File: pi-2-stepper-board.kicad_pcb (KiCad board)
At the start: 2 copper layers, 65 x 56 mm, 18 parts, among them CON1 DC12v, P1 Servo (A0), P2 Endstop1 (A1), P3 Endstop2 (A2), P4 Stepper1, P5 Stepper2, P6 COM, P7 Aux (D10 - 13), SW1 GPIO21, SW2 ON - OFF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

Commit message: Added I2C updated text
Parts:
- added REF**: Symbol_OSHW-Logo_SilkScreen, Symbols:Symbol_OSHW-Logo_SilkScreen, B.Cu at (86.0, 61.8)
- SW1: value GPIO21 -> SW_PUSH
- SW2: value ON - OFF -> SPDT
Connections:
- U1 pad 3: Net-(U1-Pad3) -> /SDA
- U1 pad 5: Net-(U1-Pad5) -> /SCL
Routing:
- net /SDA: track 0.00 -> 49.5 mm, vias 0 -> 1
- net /SCL: track 0.00 -> 33.0 mm, vias 0 -> 1
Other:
- board text added: "Copyright Mark Benson 2016 License: CC-BY-NC"
- board text added: "Designed for use with Pycupi: https://github.com/brianinnes/pycupi"
- board text added: "Rapsberry Pi 2/3 Arduino Pro Mini (3.3v @ 8MHz) Dual Stepper control brd."
- board text added: "https://github.com/MarkJB/pi-2-stepper-board"

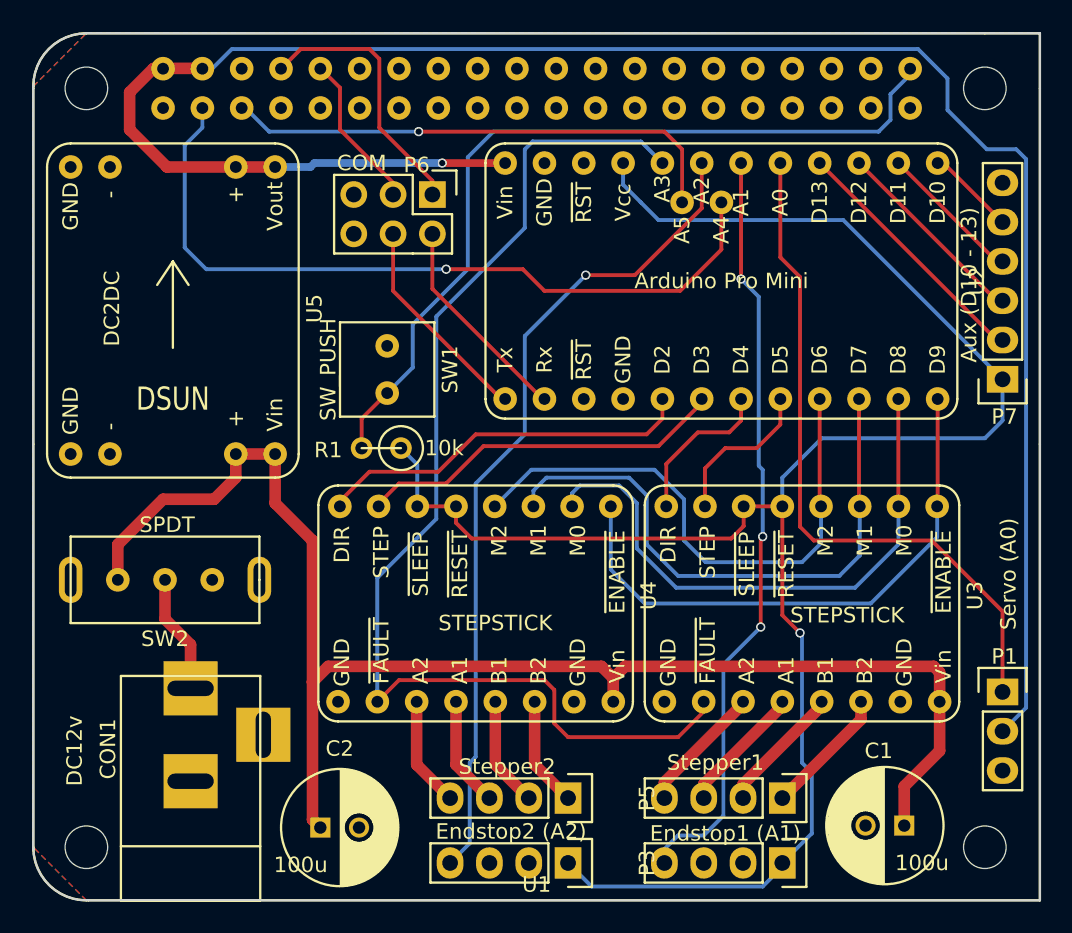
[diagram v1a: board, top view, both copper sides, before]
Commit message: Added I2C port and other fixes
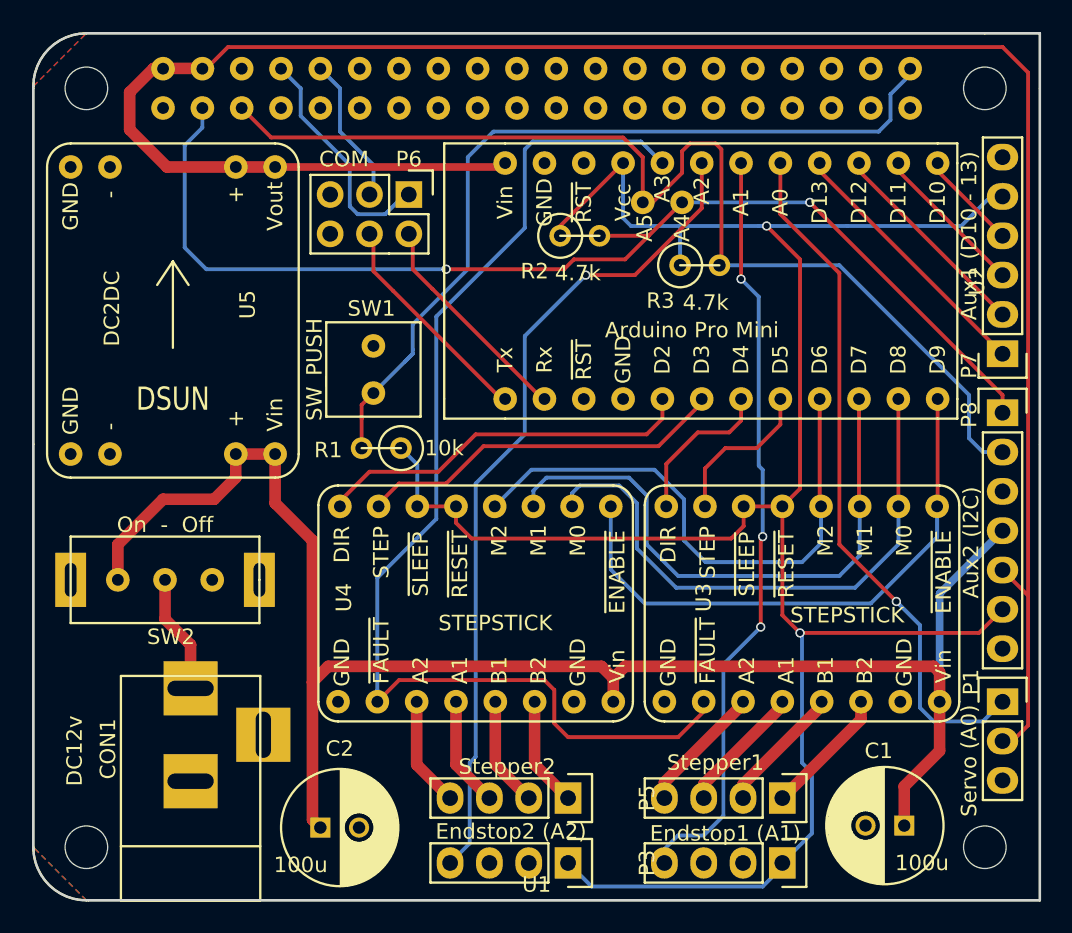
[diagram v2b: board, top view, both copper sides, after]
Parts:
- added P8: Aux2 (I2C), Pin_Headers:Pin_Header_Straight_1x07, F.Cu at (139.4, 68.6)
- added R2: 4.7k, Discret:R1, F.Cu at (112.1, 57.1)
- added R3: 4.7k, Discret:R1, F.Cu at (119.9, 59.1)
- P7: value Aux (D10 - 13) -> Aux1 (D10 - 13)
- SW2: value SPDT -> On - Off
- moved P7 1.65 mm to (139.4, 64.8)
- moved P6 1.52 mm to (101.1, 54.5)
- moved SW1 0.89 mm to (98.8, 65.8)
- moved P1 0.63 mm to (139.4, 87.2)
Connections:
- P7 pad 1: /3v3 -> /D10
- P7 pad 2: /D10 -> /D11
- P7 pad 3: /D11 -> /D12
- P7 pad 4: /D12 -> /D13
- P7 pad 5: /D13 -> /3v3
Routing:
- net /SCL: track 33.0 -> 70.5 mm, vias 1 -> 0
- net /SDA: track 49.5 -> 74.2 mm, vias 1 -> 2
- net /3v3: track 122.1 -> 142.2 mm, vias 1 -> 2
- net +12V: track 95.2 -> 107.9 mm
- net /VCC: track 128.6 -> 134.9 mm, vias 1 -> 0
- net /PiTx: track 17.3 -> 15.3 mm
- net /D13: track 5.77 -> 7.07 mm
- net /SERVO: track 44.6 -> 45.4 mm, vias 0 -> 1
- net /GPIO21: track 53.8 -> 54.5 mm
- net /D12: track 9.36 -> 10.0 mm
- net /D10: track 16.5 -> 17.2 mm
- net /D11: track 13.0 -> 13.6 mm
- net /ArdTx: track 13.8 -> 14.3 mm
- net /ArdRx: track 13.7 -> 14.3 mm
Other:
- board text added: "Designed for use with vPiP: https://github.com/brianinnes/vpip"
- board text added: "Rapsberry Pi 2/3 Arduino Pro Mini (3.3v @ 8MHz) Dual Stepper control brd"
- board text removed: "Designed for use with Pycupi: https://github.com/brianinnes/pycupi"
- board text removed: "Rapsberry Pi 2/3 Arduino Pro Mini (3.3v @ 8MHz) Dual Stepper control brd."

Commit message: Design to HAT spec
Added HAT spec board (Cable cut-outs, EEPROM, Back-feed circuit). Added
jumpers to by-pass back-feed circuit. Fixed NPTH pads. Added LED.
Removed push button pull-up resistor.

NOTE: If HAT spec back-feed circuit is not fitted, Pi & Arduino are not
powered by the DC-DC converter until either P10 or JP2 are shorted. This
also by-passes the Poly fuse F1. Here be dragons...
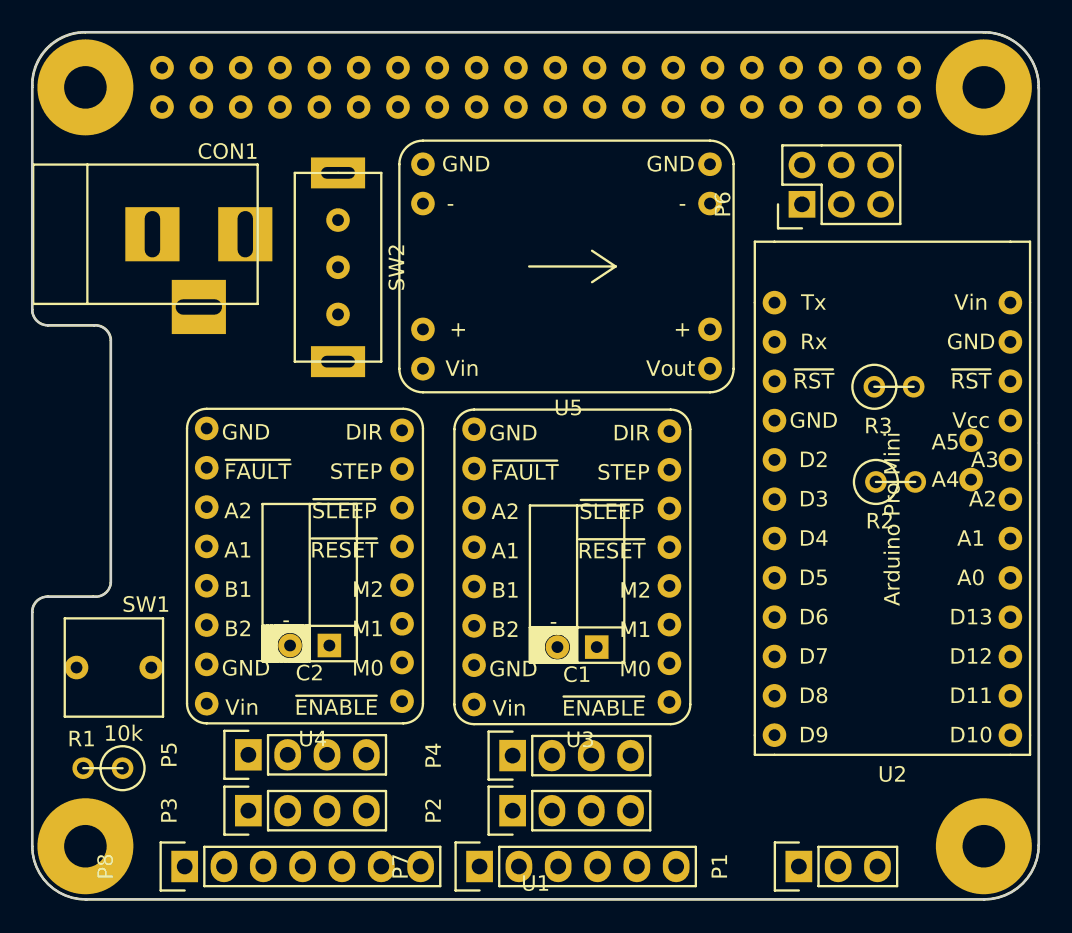
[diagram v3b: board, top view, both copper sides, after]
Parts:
- removed REF**: Symbol_OSHW-Logo_SilkScreen, Symbols:Symbol_OSHW-Logo_SilkScreen
- C1, C2: footprint Capacitors_ThroughHole:C_Radial_D7.5_L11.2_P2.5 -> custom:Cap_laying_flat_2.5mm_lead_pitch
- SW2: value On - Off -> SPDT
- U1: footprint custom:Pi_2_3 -> custom:Pi_2_3_Hat_spec
- moved P8 60.4 mm to (86.6, 97.9), turned to 90 degrees
- moved P7 47.3 mm to (105.7, 97.9), turned to 90 degrees
- moved CON1 35.6 mm to (84.3, 57.0), turned to 0 degrees
- moved R1 27.4 mm to (81.3, 91.5)
- moved R2 25.9 mm to (132.5, 73.1)
- moved U5 25.7 mm to (111.4, 59.1), turned to 0 degrees
- moved SW1 25.5 mm to (82.0, 85.0), turned to 0 degrees
- moved P6 25.4 mm to (126.5, 55.1), turned to 90 degrees
- moved SW2 23.1 mm to (96.5, 59.2), turned to 90 degrees
- moved C1 23.1 mm to (112.0, 86.0)
- moved P3 20.9 mm to (90.7, 94.3), turned to 90 degrees
- moved P5 20.8 mm to (90.7, 90.7), turned to 90 degrees
- moved U2 18.9 mm to (132.3, 75.4), turned to 0 degrees
- moved P2 17.7 mm to (107.8, 94.3), turned to 90 degrees
- moved P4 17.6 mm to (107.8, 90.7), turned to 90 degrees
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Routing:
- net /3v3: track 142.2 -> 0.00 mm, vias 2 -> 0
- net /VCC: track 134.9 -> 0.00 mm
- net +12V: track 107.9 -> 0.00 mm
- net /FAULT: track 75.8 -> 0.00 mm
- net /SDA: track 74.2 -> 0.00 mm, vias 2 -> 0
- net /SCL: track 70.5 -> 0.00 mm
- net /GPIO21: track 54.5 -> 0.00 mm
- net /ESTOP2: track 53.8 -> 0.00 mm, vias 1 -> 0
- net /ESTOP1: track 49.4 -> 0.00 mm, vias 3 -> 0
- net /SERVO: track 45.4 -> 0.00 mm, vias 1 -> 0
- net /M1: track 37.6 -> 0.00 mm
- net /M0: track 37.1 -> 0.00 mm
- net /ENABLE: track 36.8 -> 0.00 mm
- net /M2: track 36.0 -> 0.00 mm
- net /DIR2: track 24.6 -> 0.00 mm
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- removed copper zone on B.Cu, net GND
- removed copper zone on F.Cu, net GND
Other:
- outline, holes or cut-outs redrawn
- board text removed: "Copyright Mark Benson 2016 License: CC-BY-NC"
- board text removed: "DSUN"
- board text removed: "Designed for use with vPiP: https://github.com/brianinnes/vpip"
- board text removed: "Rapsberry Pi 2/3 Arduino Pro Mini (3.3v @ 8MHz) Dual Stepper control brd"
- board text removed: "https://github.com/MarkJB/pi-2-stepper-board"

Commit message: Clean up repo - board 1.0a non hat spec
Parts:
- added REF**: Symbol_OSHW-Logo_SilkScreen, Symbols:Symbol_OSHW-Logo_SilkScreen, B.Cu at (86.0, 61.8)
- C1, C2: footprint custom:Cap_laying_flat_2.5mm_lead_pitch -> Capacitors_ThroughHole:C_Radial_D7.5_L11.2_P2.5
- SW2: value SPDT -> On - Off
- U1: footprint custom:Pi_2_3_Hat_spec -> custom:Pi_2_3
- moved P8 60.4 mm to (139.4, 68.6), turned to 0 degrees
- moved P7 47.3 mm to (139.4, 64.8), turned to 180 degrees
- moved CON1 35.6 mm to (87.0, 92.6), turned to 90 degrees
- moved R1 27.4 mm to (99.3, 70.9)
- moved R2 25.9 mm to (112.1, 57.1)
- moved U5 25.7 mm to (85.9, 61.8), turned to 90 degrees
- moved SW1 25.5 mm to (98.8, 65.8), turned to 90 degrees
- moved P6 25.4 mm to (101.1, 54.5), turned to 270 degrees
- moved SW2 23.1 mm to (85.3, 79.4), turned to 0 degrees
- moved C1 23.1 mm to (133.1, 95.2)
- moved P3 20.9 mm to (111.4, 97.7), turned to 270 degrees
- moved P5 20.8 mm to (111.4, 93.5), turned to 270 degrees
- moved U2 18.9 mm to (121.3, 60.1), turned to 90 degrees
- moved P2 17.7 mm to (125.2, 97.7), turned to 270 degrees
- moved P4 17.6 mm to (125.2, 93.5), turned to 270 degrees
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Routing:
- net /3v3: track 0.00 -> 142.2 mm, vias 0 -> 2
- net /VCC: track 0.00 -> 134.9 mm
- net +12V: track 0.00 -> 107.9 mm
- net /FAULT: track 0.00 -> 75.8 mm
- net /SDA: track 0.00 -> 74.2 mm, vias 0 -> 2
- net /SCL: track 0.00 -> 70.5 mm
- net /GPIO21: track 0.00 -> 54.5 mm
- net /ESTOP2: track 0.00 -> 53.8 mm, vias 0 -> 1
- net /ESTOP1: track 0.00 -> 49.4 mm, vias 0 -> 3
- net /SERVO: track 0.00 -> 45.4 mm, vias 0 -> 1
- net /M1: track 0.00 -> 37.6 mm
- net /M0: track 0.00 -> 37.1 mm
- net /ENABLE: track 0.00 -> 36.8 mm
- net /M2: track 0.00 -> 36.0 mm
- net /DIR2: track 0.00 -> 24.6 mm
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- added copper zone on B.Cu, net GND
- added copper zone on F.Cu, net GND
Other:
- outline, holes or cut-outs redrawn
- board text added: "Copyright Mark Benson 2016 License: CC-BY 4.0"
- board text added: "DSUN"
- board text added: "Designed for use with vPiP: https://github.com/brianinnes/vpip"
- board text added: "No warranty implied or given. Use at own risk!"
- board text added: "Rapsberry Pi 2/3 Arduino Pro Mini (3.3v @ 8MHz) Dual Stepper control brd"
- board text added: "https://github.com/MarkJB/pi-2-stepper-board"
